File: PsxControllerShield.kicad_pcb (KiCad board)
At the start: 2 copper layers, 68.6 x 53.3 mm, 27 parts, among them J1 TO_PSX_PAD, J2 OSHW_LOGO, Q1 BSS138, Q2 BSS138, Q3 BSS138, Q4 BSS138, Q5 BSS138, U1 LM1117-3.3

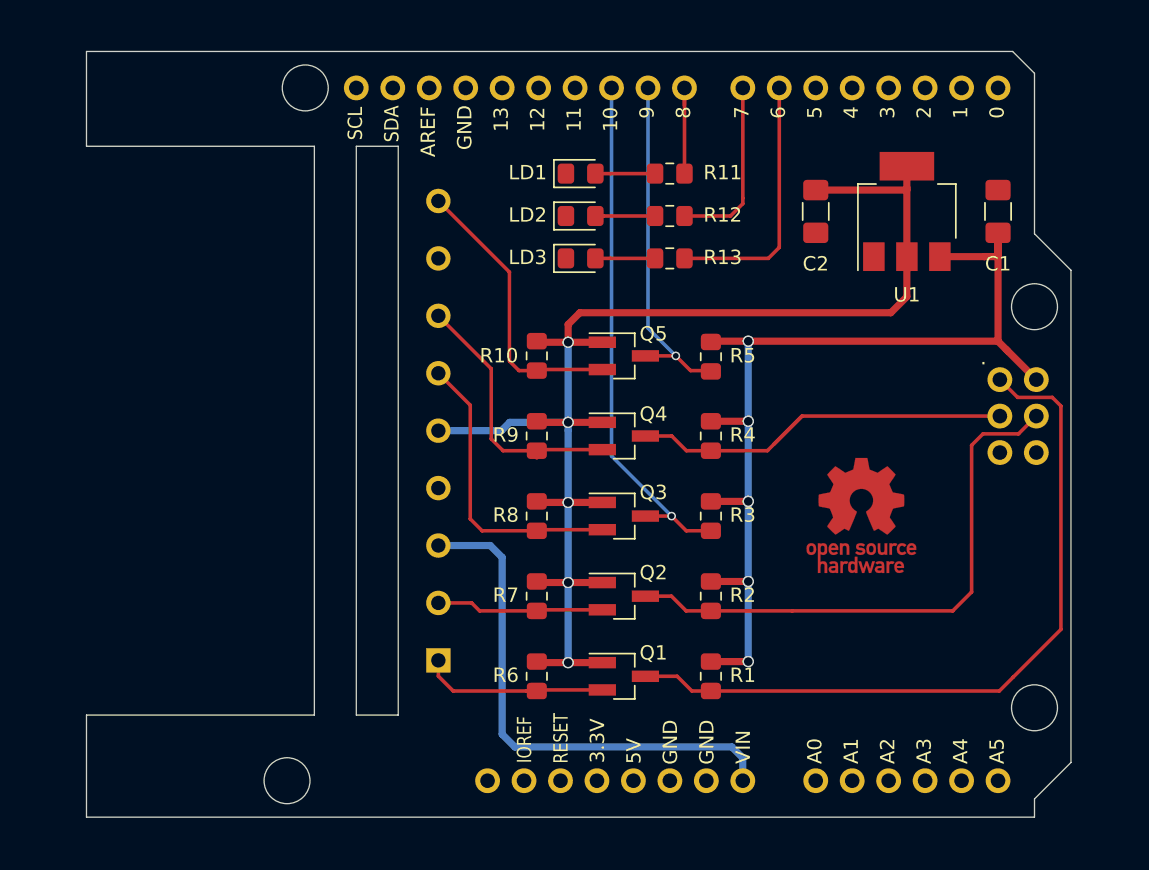
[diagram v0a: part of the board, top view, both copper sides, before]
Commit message: Ready for V2 (probably) Changes wrt V1: - Added 7.5V regulator for motors (I still think they're probably fine with 9V, but we want to be 100% rigorous with this board) - Move PSX connector towards board edge - Allow for actual tantalum caps - Reroute tracks - Switch all pullups to 1k, after measuring on a real PsOne
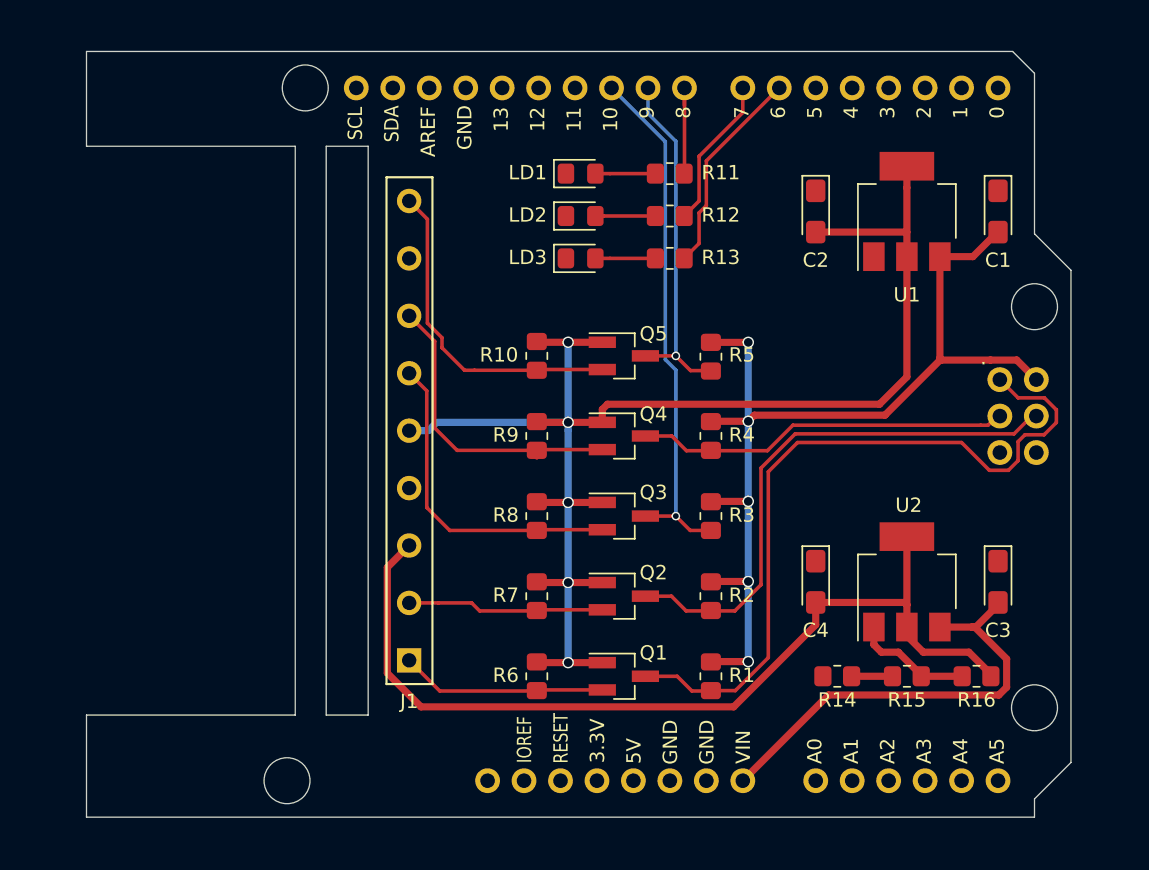
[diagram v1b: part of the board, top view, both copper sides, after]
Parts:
- added C3: 10u, Capacitor_Tantalum_SMD:CP_EIA-3216-18_Kemet-A_Pad1.58x1.35mm_HandSolder, F.Cu at (177.4, 104.1)
- added C4: 10u, Capacitor_Tantalum_SMD:CP_EIA-3216-18_Kemet-A_Pad1.58x1.35mm_HandSolder, F.Cu at (164.7, 104.1)
- added R14: 100, Resistor_SMD:R_0805_2012Metric_Pad1.20x1.40mm_HandSolder, F.Cu at (166.2, 110.6)
- added R15: 1k, Resistor_SMD:R_0805_2012Metric_Pad1.20x1.40mm_HandSolder, F.Cu at (171.1, 110.6)
- added R16: 220, Resistor_SMD:R_0805_2012Metric_Pad1.20x1.40mm_HandSolder, F.Cu at (175.9, 110.6)
- added U2: LM1117-ADJ, Package_TO_SOT_SMD:SOT-223-3_TabPin2, F.Cu at (171.1, 104.1)
- C1, C2: footprint Capacitor_SMD:C_1206_3216Metric_Pad1.42x1.75mm_HandSolder -> Capacitor_Tantalum_SMD:CP_EIA-3216-18_Kemet-A_Pad1.58x1.35mm_HandSolder
- J2: footprint Symbol:OSHW-Logo_7.5x8mm_Copper -> Symbol:OSHW-Logo_7.5x8mm_SilkScreen; moved to B.Cu
- R1, R10, R2, R3, R4, R5, R6, R7, R8, R9: value 10k -> 1k; footprint Resistor_SMD:R_0805_2012Metric_Pad1.15x1.40mm_HandSolder -> Resistor_SMD:R_0805_2012Metric_Pad1.20x1.40mm_HandSolder
- R11, R12, R13: footprint Resistor_SMD:R_0805_2012Metric_Pad1.15x1.40mm_HandSolder -> Resistor_SMD:R_0805_2012Metric_Pad1.20x1.40mm_HandSolder
- moved J1 12.0 mm to (136.4, 93.5)
- moved J2 7.86 mm to (160.0, 99.4), turned to 180 degrees
- turned C2 to 270 degrees
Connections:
- J1 pad 3: +9V -> +7.5V
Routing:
- net +7.5V: track 0.00 -> 64.5 mm
- net Net-(R15-Pad1): track 0.00 -> 8.34 mm
- net +3V3: track 95.7 -> 100.7 mm
- net +9V: track 36.1 -> 31.3 mm
- net /led3: track 18.0 -> 14.6 mm
- net /ps_ack_3v3: track 20.0 -> 23.0 mm
- net Net-(R14-Pad1): track 0.00 -> 2.85 mm
- net /ps_clk: track 28.9 -> 26.2 mm
- net /ps_clk_3v3: track 18.3 -> 21.0 mm
- net /ps_attn_3v3: track 20.6 -> 22.8 mm
- net /ps_cmd_3v3: track 11.7 -> 13.7 mm
- net /led2: track 12.5 -> 10.6 mm
- net /ps_data_3v3: track 13.0 -> 14.4 mm
- net /ps_cmd: track 39.3 -> 38.0 mm
- net /ps_data: track 51.7 -> 52.5 mm
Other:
- outline, holes or cut-outs redrawn
- rule pad_to_mask_clearance: 0.051 -> 0
- board text added: "This shield drives the PSX controller through the SPI bus. It also uses pin 9 for the ACK signal and pin 10 for ATTN. Leds are on pins 6/7/8. It also powers the vibration motors with 7.5V. Thus it is recommended to power the Arduino board with at least 9.5V through the barrel jack. IMPORTANT: Only use with Arduino boards that work at 5V!"
- board text added: "V2"
- board text removed: "This shield drives the PSX controller through the SPI bus. It also uses pin 9 for the ACK signal and pin 10 for ATTN. Leds are on pins 6/7/8. It also powers the vibration motors from the VIN pin. Thus it is recommended to power the Arduino board with exactly 9V through the barrel jack."
- board text removed: "V1"

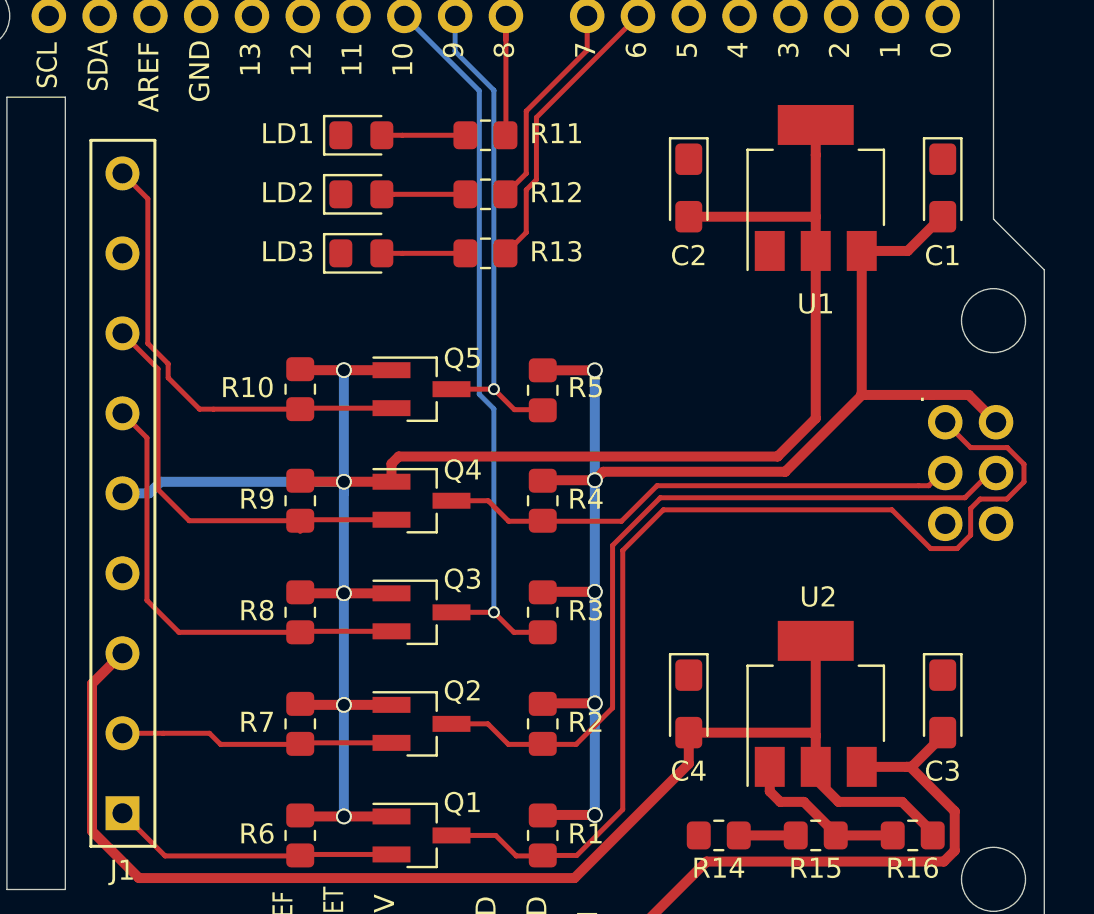
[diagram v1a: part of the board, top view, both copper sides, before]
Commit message: Use larger footprint for tantalums
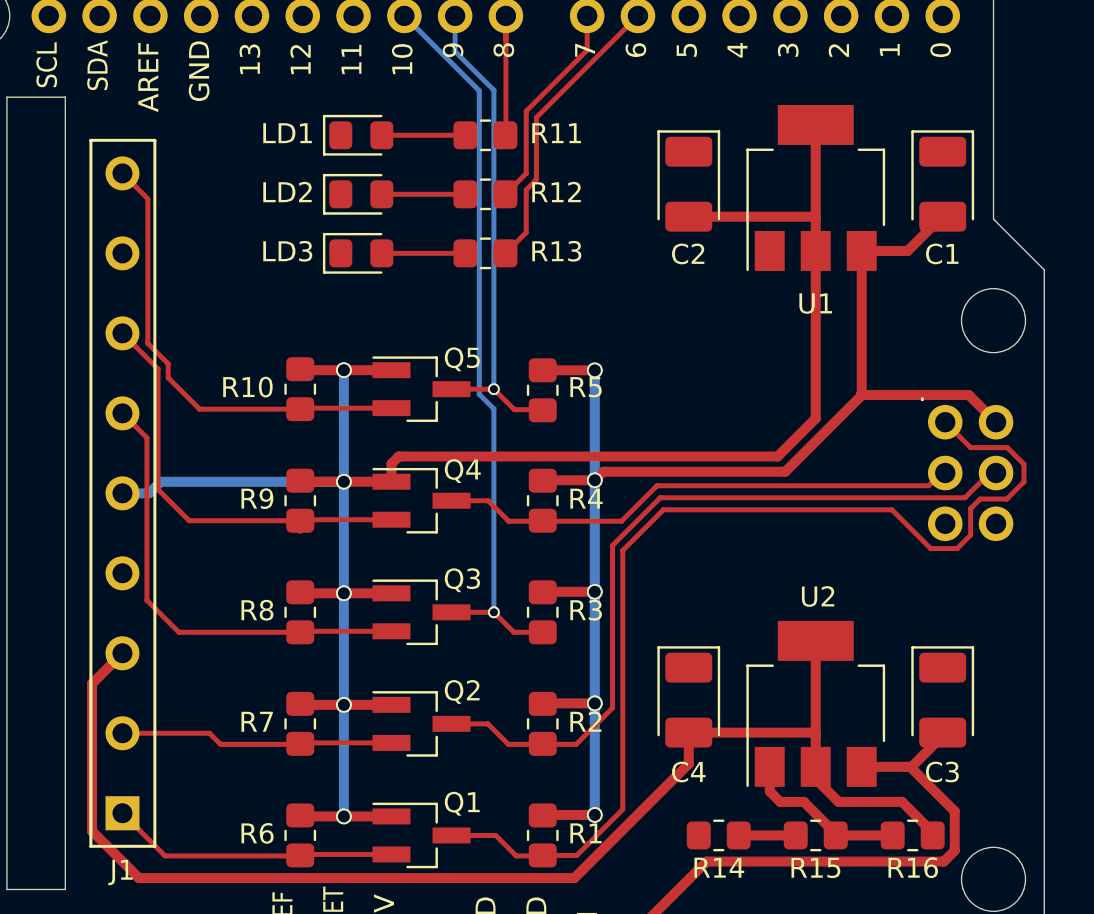
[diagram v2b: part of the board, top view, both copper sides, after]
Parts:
- C1, C2, C3, C4: footprint Capacitor_Tantalum_SMD:CP_EIA-3216-18_Kemet-A_Pad1.58x1.35mm_HandSolder -> Capacitor_Tantalum_SMD:CP_EIA-3528-12_Kemet-T_Pad1.50x2.35mm_HandSolder
- moved C1 0.19 mm to (177.4, 78.1)
- moved C2 0.19 mm to (164.7, 78.1)
- moved C3 0.19 mm to (177.4, 103.9)
- moved C4 0.19 mm to (164.7, 103.9)

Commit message: Move tracks around
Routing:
- net /ps_data: track 52.5 -> 50.5 mm
- net +3V3: track 100.7 -> 99.8 mm
- net +7.5V: track 64.6 -> 65.5 mm
- net GND: vias 0 -> 4

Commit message: Add ability to select ACK pin between 3 and 9
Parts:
- added J3: JMP_ACK, Connector_PinHeader_2.54mm:PinHeader_1x03_P2.54mm_Vertical, F.Cu at (159.6, 80.8)
- moved J2 24.9 mm to (171.1, 77.1)
- moved LD1 2.03 mm to (146.3, 75.6)
- moved LD2 2.03 mm to (146.3, 78.6)
- moved LD3 2.03 mm to (146.3, 81.5)
- moved R11 2.03 mm to (152.5, 75.6)
- moved R12 2.03 mm to (152.5, 78.6)
- moved R13 2.03 mm to (152.5, 81.5)
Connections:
- XA1 pad D3: (no net) -> Net-(J3-Pad1)
- XA1 pad D9: /ps_ack -> Net-(J3-Pad3)
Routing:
- net Net-(J3-Pad1): track 0.00 -> 21.2 mm
- net Net-(J3-Pad3): track 0.00 -> 11.5 mm
- net /ps_ack: track 24.5 -> 19.7 mm
- net /led3: track 14.6 -> 16.4 mm
- net /ps_attn: track 36.7 -> 37.7 mm
- net /led2: track 10.6 -> 11.5 mm
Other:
- board text added: "ACK PIN"
- board text added: "This shield drives the PSX controller through the SPI bus. It also uses pin 10 for ATTN. The ACK pin can be selected between pin 3 and pin 9. Leds are on pins 6/7/8. It also powers the vibration motors with 7.5V. Thus it is recommended to power the Arduino board with at least 9.5V through the barrel jack. IMPORTANT: Only use with Arduino boards that work at 5V!"
- board text removed: "This shield drives the PSX controller through the SPI bus. It also uses pin 9 for the ACK signal and pin 10 for ATTN. Leds are on pins 6/7/8. It also powers the vibration motors with 7.5V. Thus it is recommended to power the Arduino board with at least 9.5V through the barrel jack. IMPORTANT: Only use with Arduino boards that work at 5V!"

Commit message: Align some stuff
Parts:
- moved LD3 0.96 mm to (146.3, 80.6)
- moved R13 0.96 mm to (152.5, 80.6)
- moved LD2 0.55 mm to (146.3, 78.0)
- moved R12 0.55 mm to (152.5, 78.0)
- moved J3 0.20 mm to (159.6, 80.6)
- moved LD1 0.13 mm to (146.3, 75.5)
- moved R11 0.13 mm to (152.5, 75.5)
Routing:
- net /led3: track 16.4 -> 15.5 mm
- net GND: vias 4 -> 0
